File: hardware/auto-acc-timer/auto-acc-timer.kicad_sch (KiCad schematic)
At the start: 12 parts, among them J1 Conn_01x07_Pin, J3 Conn_02x03_Odd_Even, Q1 BRC108, Q2 BSS83P, U1 ATtiny85-20S, U2 MCP1703Ax-330xxDB

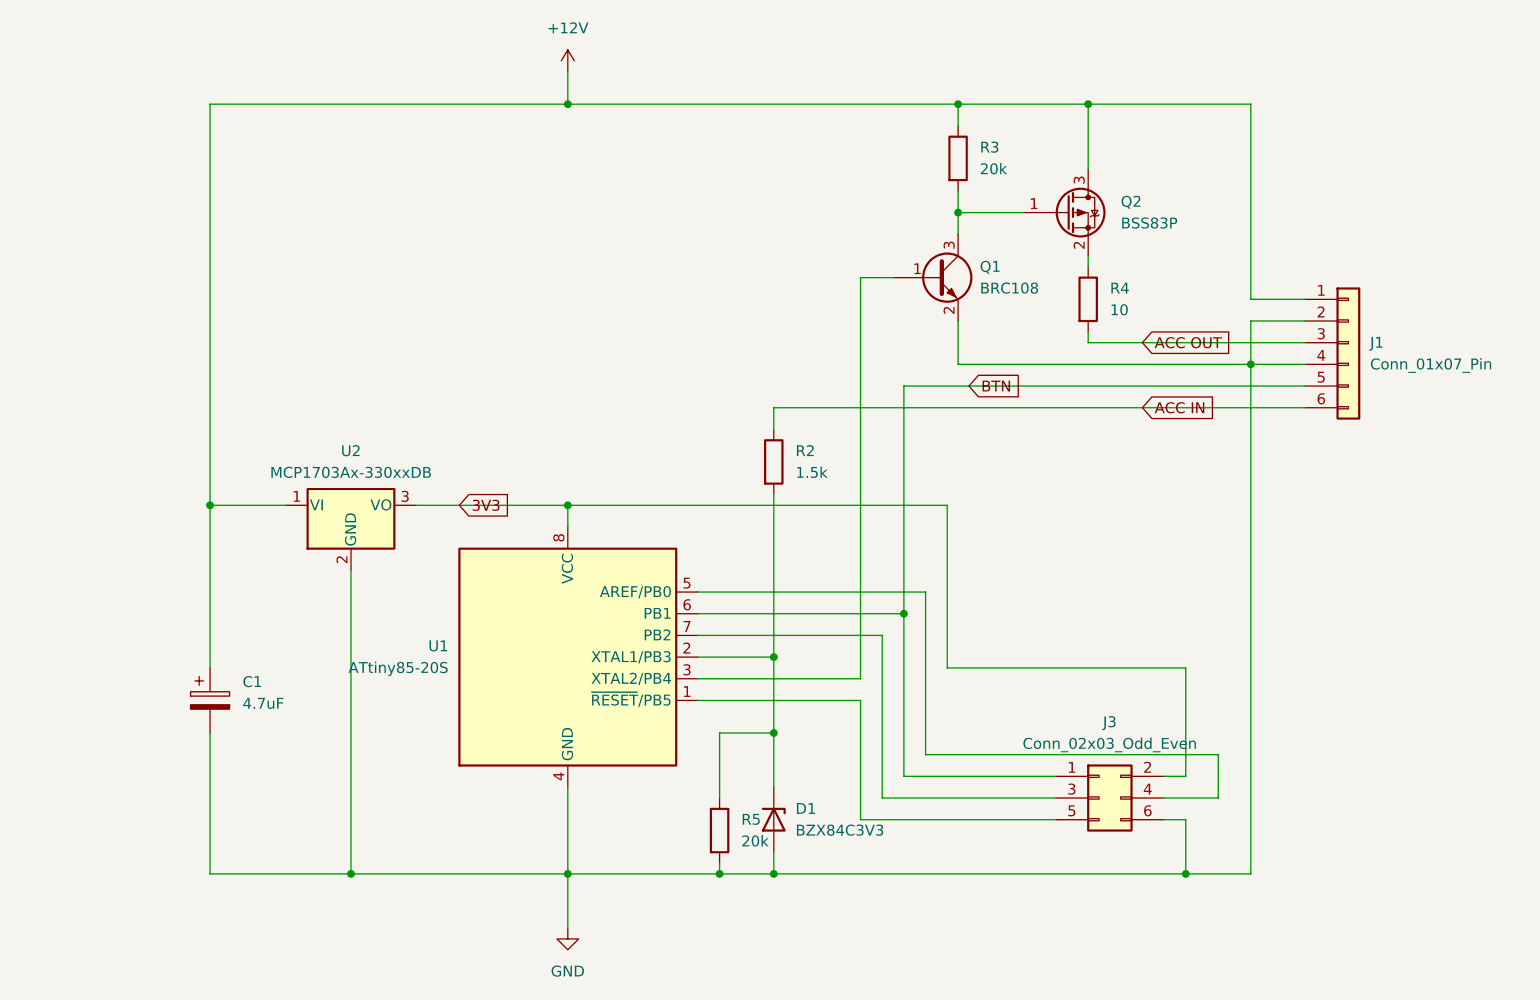
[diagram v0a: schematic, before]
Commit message: Fix wrong connection of Q2, move to KiCAD v 9
The Q2 FET was connected the wrong way, fix that. and Move to KiCAD
version9
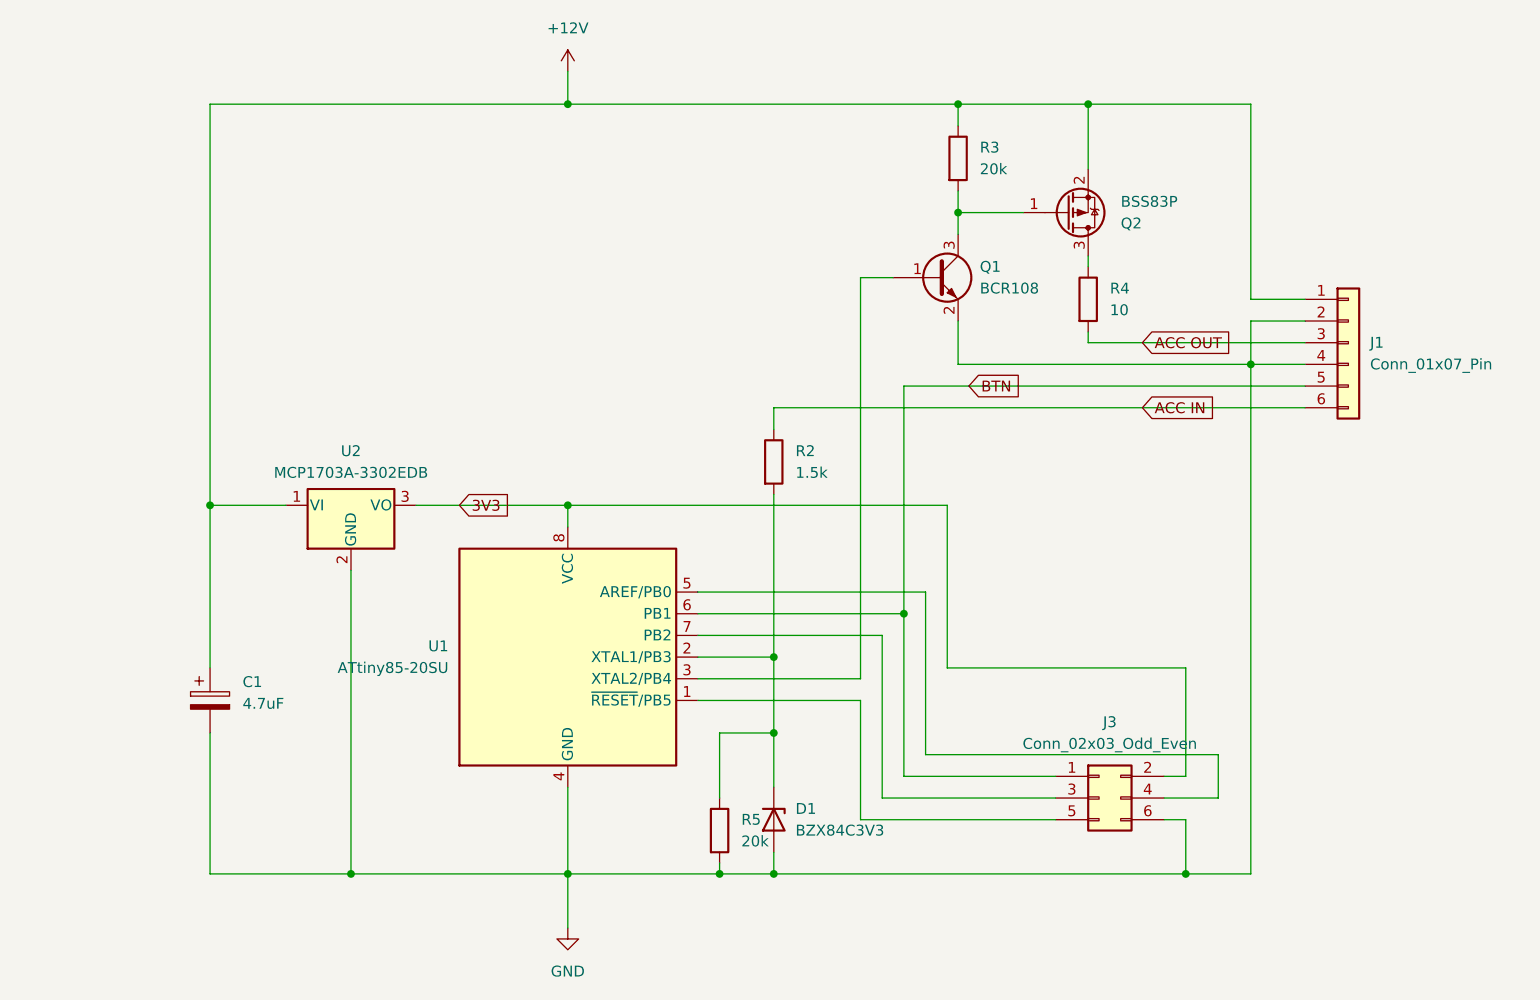
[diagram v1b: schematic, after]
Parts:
- Q1: value BRC108 -> BCR108
- U1: value ATtiny85-20S -> ATtiny85-20SU; footprint Package_SO:SOIC-8W_5.3x5.3mm_P1.27mm -> Package_SO:SOIC-8_5.3x5.3mm_P1.27mm
- U2: value MCP1703Ax-330xxDB -> MCP1703A-3302EDB
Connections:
- net +12V: now also Q2.2 (S); no longer Q2.3 (D)
- net at R4.1: now also Q2.3 (D); no longer Q2.2 (S)

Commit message: Rev 2 Hardware
Add capacitor 1uF at 3.3V rail
Add resistor to pull RESET high
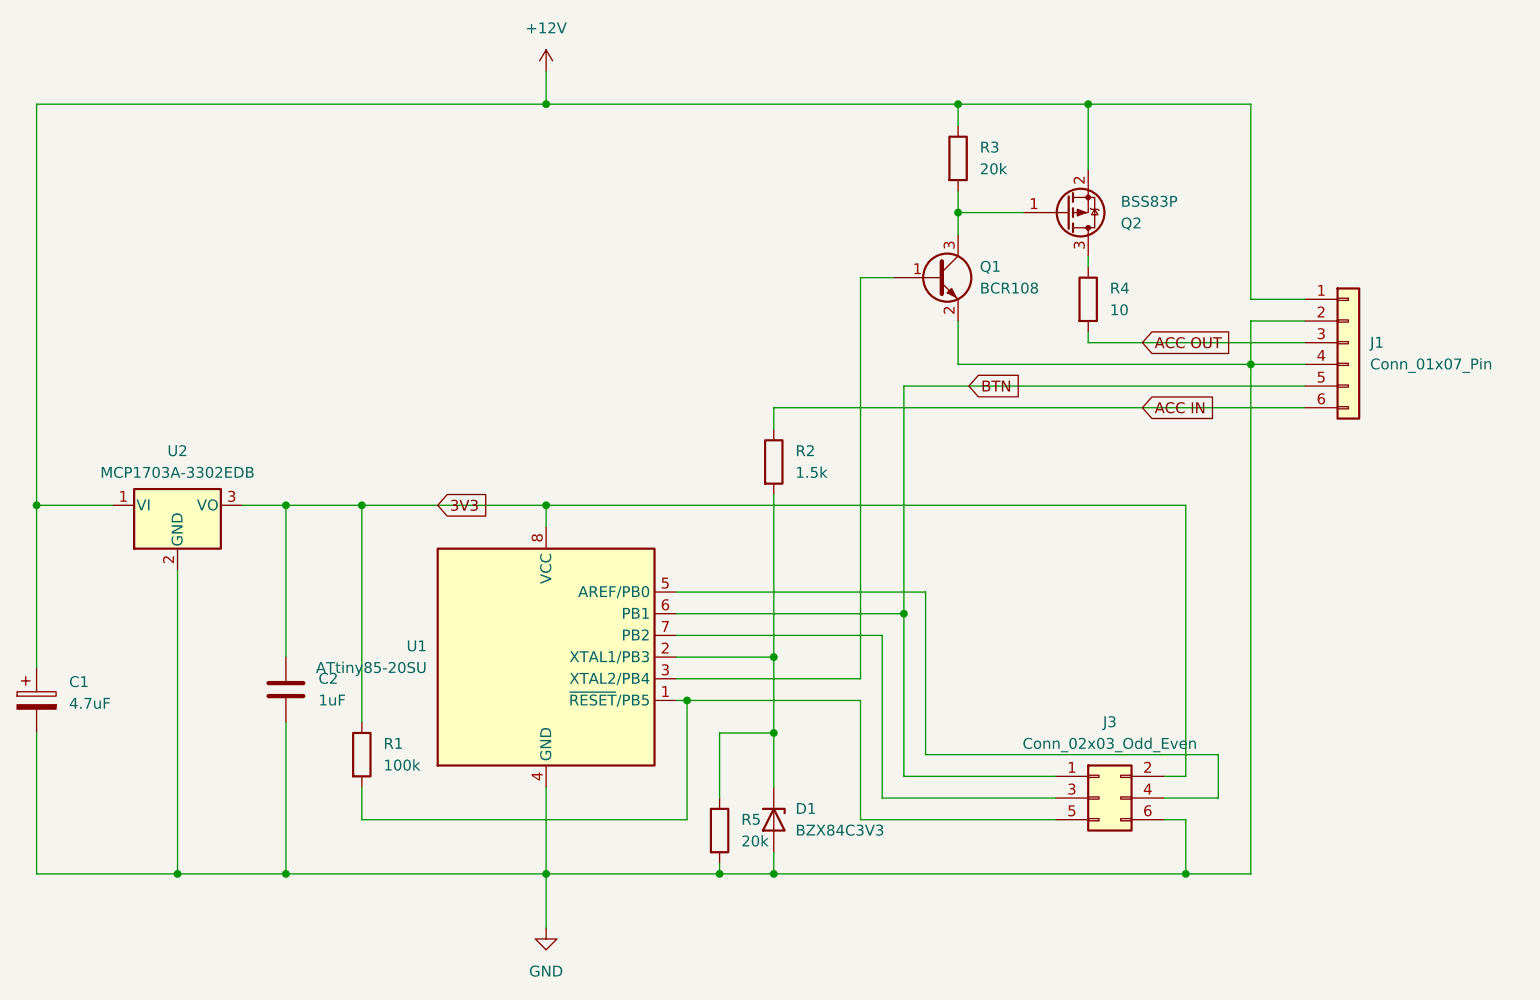
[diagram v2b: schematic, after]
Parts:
- added C2: 1uF, Capacitor_SMD:C_0805_2012Metric_Pad1.18x1.45mm_HandSolder, symbol Device:C
- added R1: 100k, Resistor_SMD:R_0805_2012Metric_Pad1.20x1.40mm_HandSolder, symbol Device:R
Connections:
- net 3V3: now also C2.1, R1.1
- net GND: now also C2.2
- net at J3.5 (Pin_5), U1.1 (~{RESET}/PB5): now also R1.2
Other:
- moved on the sheet: C1, U1, U2
